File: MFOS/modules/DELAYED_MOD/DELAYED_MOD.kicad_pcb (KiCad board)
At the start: 2 copper layers, 160 x 100 mm, 100 parts, among them J1 Card Connector, J10 -15V, J2 MonoJack, J3 MonoJack, J4 MonoJack, J6 GATE, J7 GATE SELECT, J8 +15V, J9 GND, Q1 2N3906, Q2 2N5457, Q3 2N3904, U1 TL074, U2 LM13700, U3 TL072, X1 WireConnector, X10 WireConnector, X11 WireConnector, X12 WireConnector, X13 WireConnector, X14 WireConnector, X15 WireConnector, X16 WireConnector, X17 WireConnector, X18 WireConnector, X19 WireConnector, X2 WireConnector, X20 WireConnector, X21 WireConnector, X22 WireConnector, X3 WireConnector, X5 WireConnector, X6 WireConnector, X7 WireConnector, X8 WireConnector, X9 WireConnector

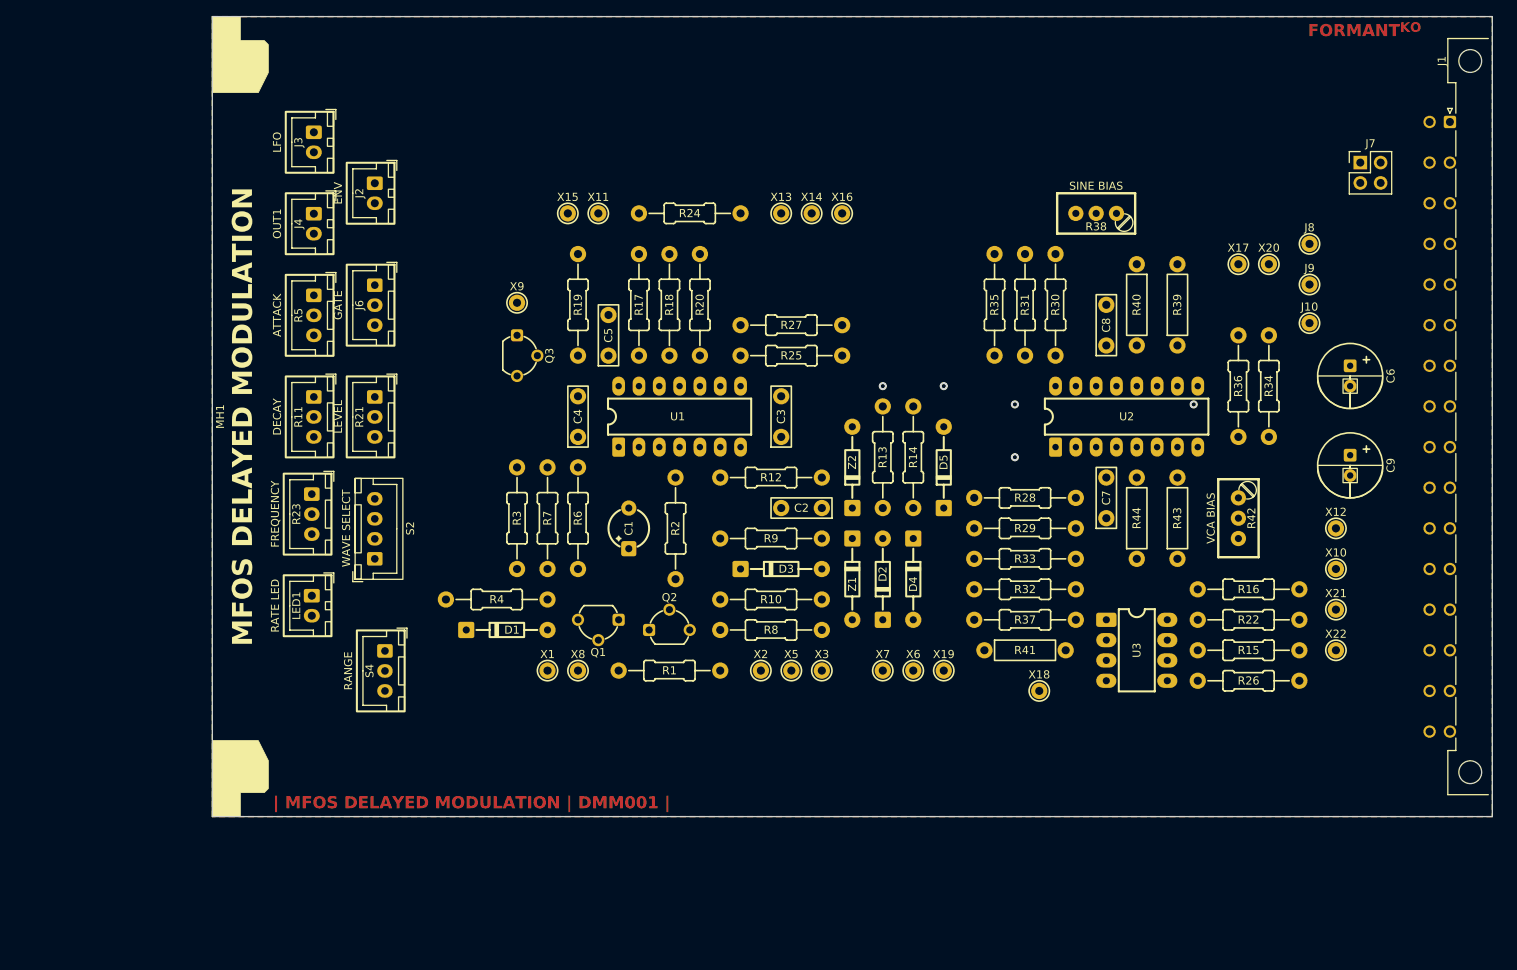
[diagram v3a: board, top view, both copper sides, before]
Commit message: meter bezels svg added
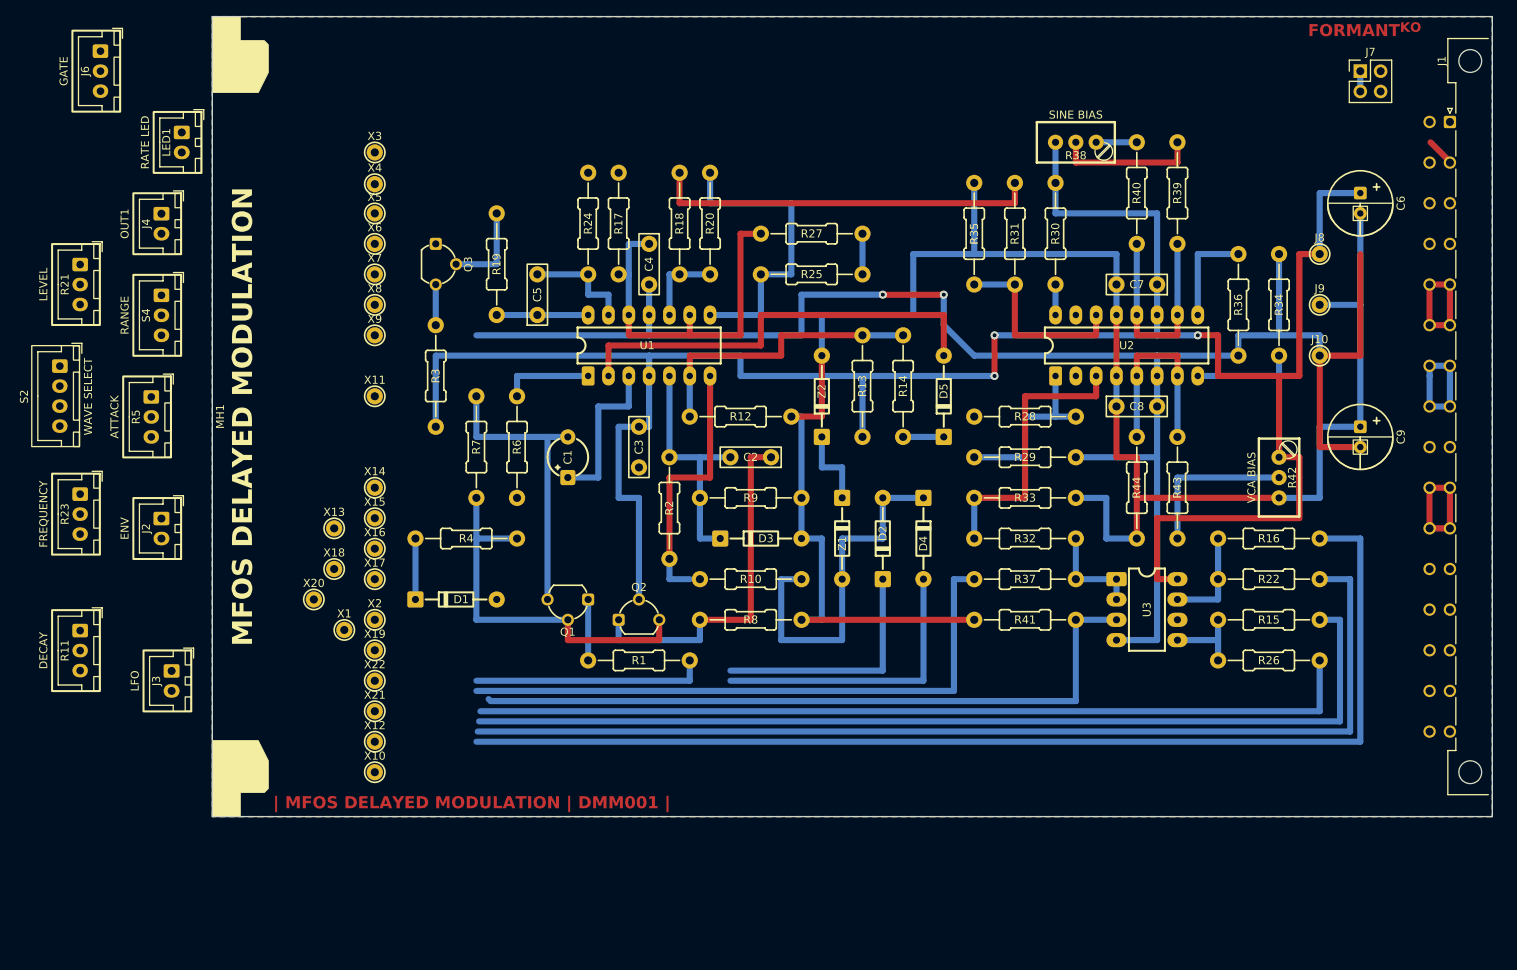
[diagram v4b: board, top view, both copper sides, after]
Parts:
- added X4: WireConnector, FormantKO:Wire_1x01_D40mil_OD80mil, F.Cu at (75.3, 65.9)
- R39, R40, R41, R43, R44: footprint FormantKO:R_Axial_Horizontal_P400mil -> FormantKO:R_Axial_Horizontal_P500mil
- moved X20 126.5 mm to (67.7, 117.9)
- moved X12 123.1 mm to (75.3, 135.6)
- moved X10 122.8 mm to (75.3, 139.4)
- moved X21 120.8 mm to (75.3, 131.8)
- moved X22 120.2 mm to (75.3, 128.0)
- moved X17 114.9 mm to (75.3, 115.3)
- moved X18 89.4 mm to (70.2, 114.0)
- moved X6 85.9 mm to (75.3, 73.4)
- moved X3 85.5 mm to (75.3, 62.0)
- moved X7 80.5 mm to (75.3, 77.2)
- moved X5 77.3 mm to (75.3, 69.6)
- moved X16 71.9 mm to (75.3, 111.5)
- moved X19 71.2 mm to (75.3, 124.2)
- moved J3 69.6 mm to (49.9, 128.0)
- moved X13 68.4 mm to (70.2, 109.0)
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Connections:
- J7 pad 1: GATE1 -> IGATE
- J7 pad 2: GATE2 -> GATE1
- J7 pad 4: IGATE -> GATE2
- R29 pad 1: IEV -> Net-(R28-Pad1)
- R32 pad 1: LFO -> ILFO
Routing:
- net GND: track 0.00 -> 309.9 mm
- net +15V: track 0.00 -> 304.8 mm
- net -15V: track 0.00 -> 274.6 mm
- net OUT1: track 0.00 -> 141.0 mm
- net OUT2: track 0.00 -> 131.9 mm
- net Net-(R15-Pad1): track 0.00 -> 122.9 mm
- net Net-(S4-c): track 0.00 -> 111.3 mm
- net Net-(S2-C): track 0.00 -> 88.8 mm
- net LFO: track 0.00 -> 76.2 mm
- net IENV: track 0.00 -> 66.0 mm
- net TRIANGLE: track 0.00 -> 59.7 mm
- net Net-(Q1-B): track 0.00 -> 48.3 mm
- net Net-(D2-A): track 0.00 -> 45.7 mm
- net Net-(Q2-D): track 0.00 -> 44.4 mm
- net Net-(R20-Pad2): track 0.00 -> 38.1 mm
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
